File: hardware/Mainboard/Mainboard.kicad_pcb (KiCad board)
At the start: 2 copper layers, 160 x 160 mm, 83 parts, among them IC1 74HC138, IC10 FT232RL, IC11 TL7702A, IC2 W65C02, IC3 74HC00, IC4 SYSTEM ROM, IC5 W65C22, IC6 RAM, IC7 W65C22, IC8 W65C51, IC9 74HC148, SW1 CARRIER, SW2 PORT B, SW3 INTERRUPT, SW4 CLOCK INPUT, SW5 NMI, SW6 FT232 RESET, SW7 RESET, T1 BC546, U1 R-785.0-1.0, X1 EXPANSION, X2 TIMER, X3 KEYBOARD, X4 EXT. CLOCK, X5 SERIAL, X6 GND, X7 DC IN, X8 PORT B

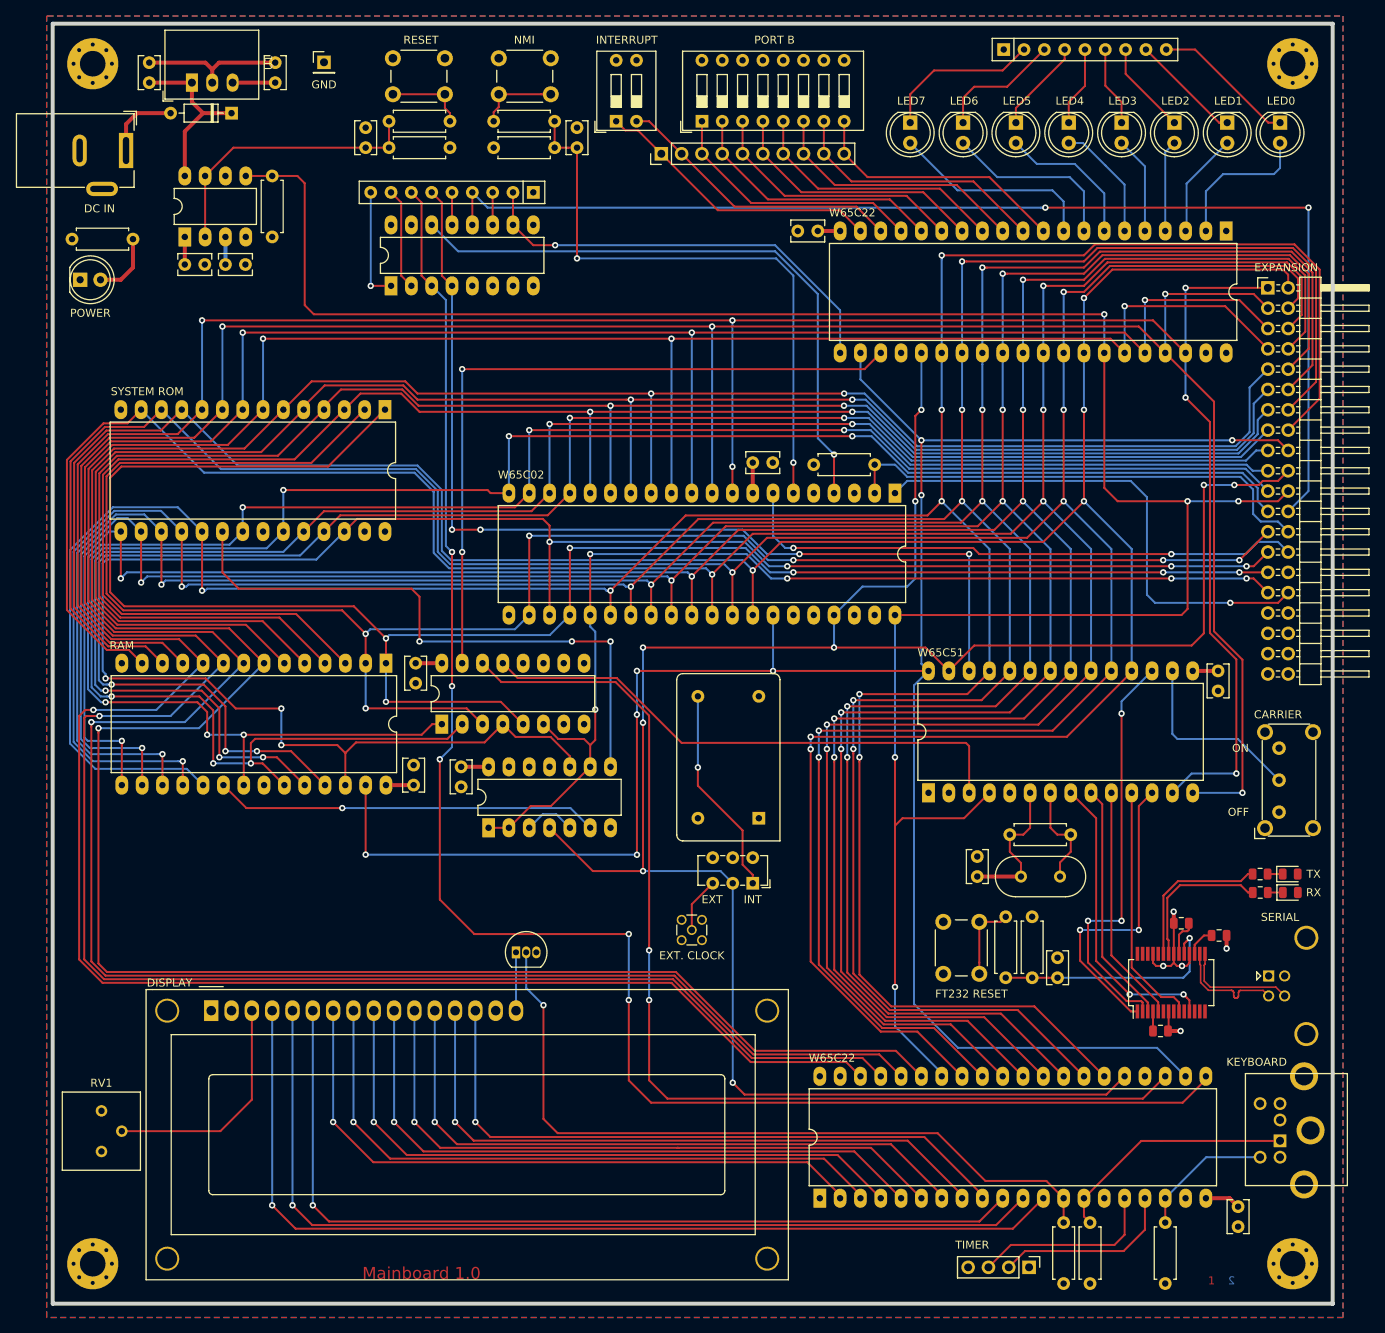
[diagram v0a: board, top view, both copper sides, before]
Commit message: Hardware: 	- Add pull up resistor for PB
Documentation:
	- Add more datasheets
	- Update documentation

Misc:
	- Rename CHANGELOG
	- Remove old files

Signed-off-by: Daniel Kampert <DanielKampert@kampis-elektroecke.de>
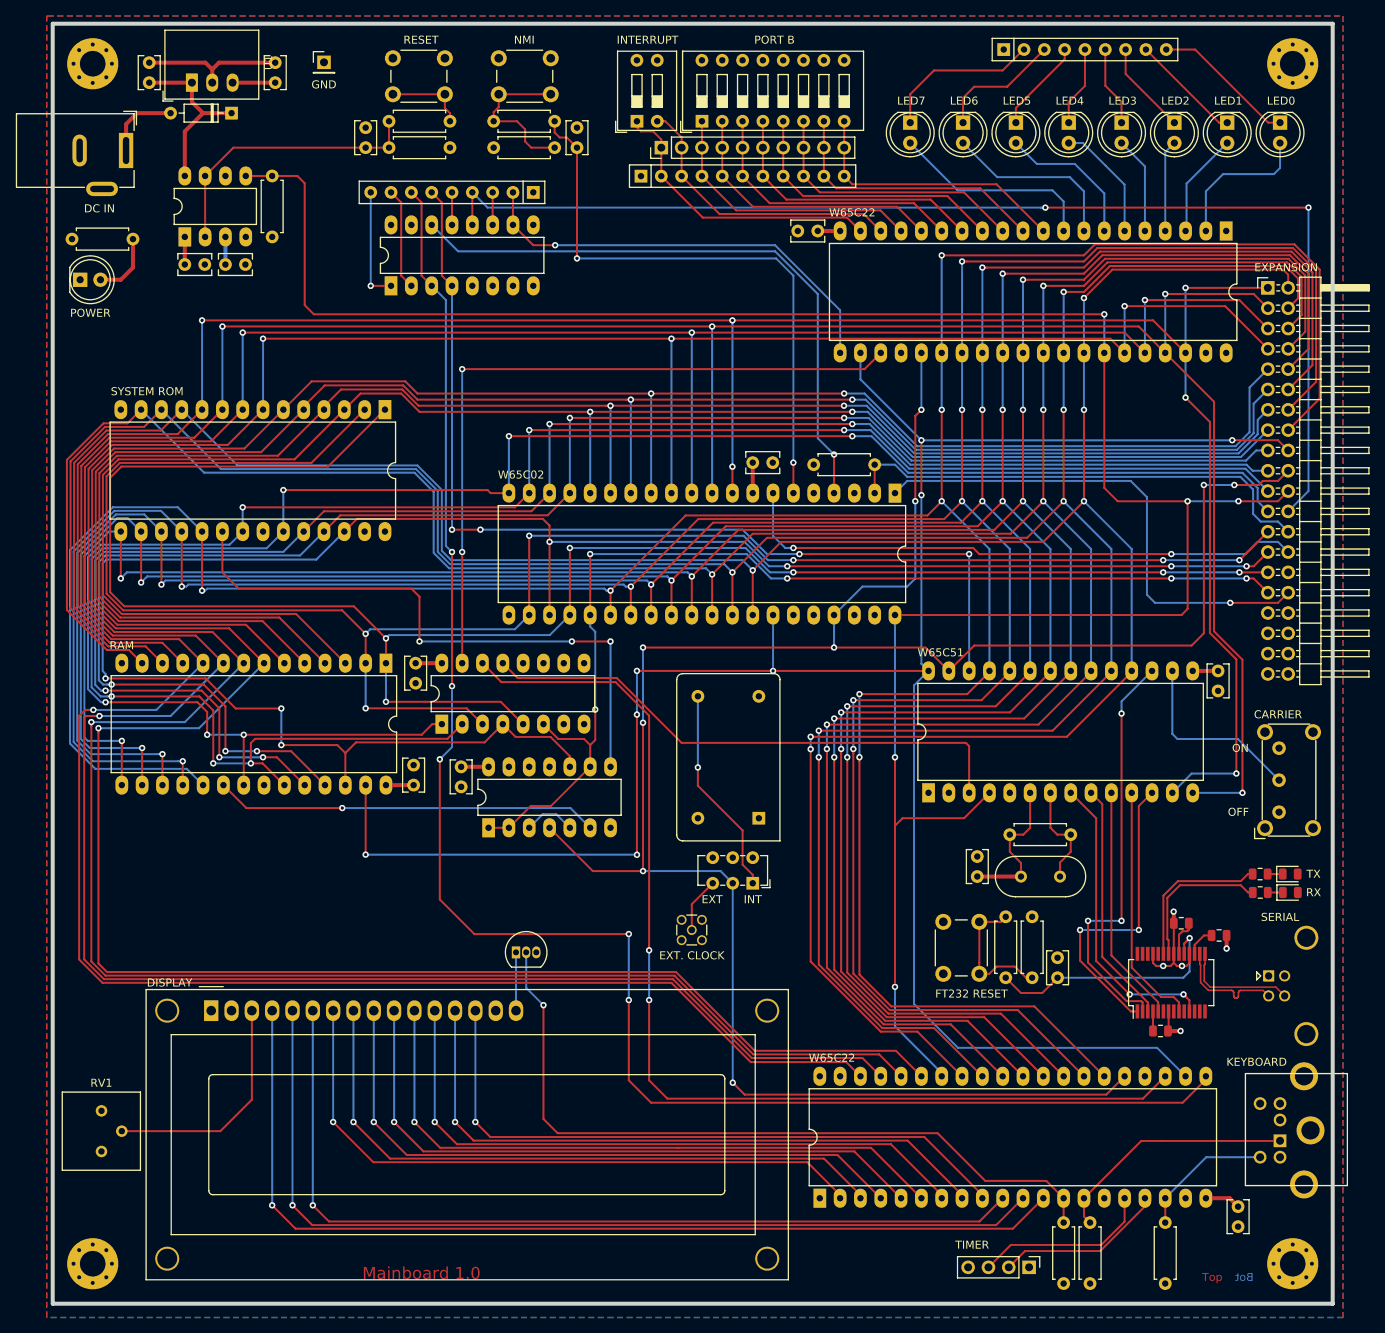
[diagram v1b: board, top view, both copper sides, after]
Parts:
- added RN1: 4k7, Resistor_THT:R_Array_SIP11, F.Cu at (211.6, 70.4)
- R1: value 4,7k -> 4k7
- moved SW3 2.59 mm to (211.1, 63.5)
- moved X1 0.76 mm to (214.1, 66.8)
- renumbered C2 to C1, C1 to C2, R9 to R10, R14 to R11, R10 to R12, R11 to R13, R15 to R14, R12 to R15, R13 to R7, R7 to R8, R8 to R9, RN1 to RN2, RN2 to RN3, X8 to X1, X1 to X2, X2 to X3, X3 to X4, X4 to X5, X5 to X6, X6 to X7, X7 to X8
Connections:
- IC1 pad 10: (no net) -> Net-(IC1-Pad10)
- IC1 pad 11: (no net) -> Net-(IC1-Pad11)
- IC1 pad 12: (no net) -> Net-(IC1-Pad12)
- IC1 pad 7: (no net) -> Net-(IC1-Pad7)
- IC1 pad 9: (no net) -> Net-(IC1-Pad9)
- IC10 pad 10: (no net) -> Net-(IC10-Pad10)
- IC10 pad 12: (no net) -> Net-(IC10-Pad12)
- IC10 pad 13: (no net) -> Net-(IC10-Pad13)
- IC10 pad 14: (no net) -> Net-(IC10-Pad14)
- IC10 pad 26: (no net) -> Net-(IC10-Pad26)
- IC10 pad 27: (no net) -> Net-(IC10-Pad27)
- IC10 pad 28: (no net) -> Net-(IC10-Pad28)
- IC10 pad 6: (no net) -> Net-(IC10-Pad6)
- IC11 pad 6: (no net) -> Net-(IC11-Pad6)
- IC2 pad 3: (no net) -> Net-(IC2-Pad3)
- IC2 pad 35: (no net) -> Net-(IC2-Pad35)
- IC2 pad 39: (no net) -> Net-(IC2-Pad39)
- IC2 pad 5: (no net) -> Net-(IC2-Pad5)
- IC5 pad 15: (no net) -> Net-(IC5-Pad15)
- IC5 pad 19: (no net) -> Net-(IC5-Pad19)
- IC5 pad 39: (no net) -> Net-(IC5-Pad39)
- IC5 pad 40: (no net) -> Net-(IC5-Pad40)
- IC7 pad 39: (no net) -> Net-(IC7-Pad39)
- IC7 pad 40: (no net) -> Net-(IC7-Pad40)
- IC8 pad 5: (no net) -> Net-(IC8-Pad5)
- IC9 pad 15: (no net) -> Net-(IC9-Pad15)
- IC9 pad 6: (no net) -> Net-(IC9-Pad6)
- IC9 pad 7: (no net) -> Net-(IC9-Pad7)
- IC9 pad 9: (no net) -> Net-(IC9-Pad9)
- R10 pad 2: /Supply/~Reset_FT232 -> Net-(R10-Pad2)
- R11 pad 2: Net-(R14-Pad2) (its old number) -> Net-(R10-Pad2)
- R6 pad 2: /IRQ/~NMI -> Net-(R6-Pad2)
- R7 pad 2: Net-(R13-Pad2) -> Net-(R6-Pad2)
- RV1 pad 3: (no net) -> Net-(RV1-Pad3)
- SW5 pad 2: Net-(R13-Pad2) -> Net-(R6-Pad2)
- SW6 pad 2: Net-(R14-Pad2) (its old number) -> Net-(R10-Pad2)
- X2 pad 30: (no net) -> Net-(X2-Pad30)
- X2 pad 33: (no net) -> Net-(X2-Pad33)
- X2 pad 34: (no net) -> Net-(X2-Pad34)
- X2 pad 35: (no net) -> Net-(X2-Pad35)
- X2 pad 36: (no net) -> Net-(X2-Pad36)
- X2 pad 37: (no net) -> Net-(X2-Pad37)
- X2 pad 38: (no net) -> Net-(X2-Pad38)
- X4 pad 2: (no net) -> Net-(X4-Pad2)
- X4 pad 6: (no net) -> Net-(X4-Pad6)
- X6 pad 1: (no net) -> Net-(X6-Pad1)
- XTAL1 pad 1: (no net) -> Net-(XTAL1-Pad1)
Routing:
- net Net-(R6-Pad2): track 0.00 -> 20.0 mm
- net Net-(R10-Pad2): track 0.00 -> 17.6 mm
- net Net-(R13-Pad2): track 10.1 -> 0.00 mm
- net Net-(R14-Pad2) (its old number): track 10.1 -> 0.00 mm
- net /LCD / PS2/Timer0: track 22.9 -> 21.2 mm
- net /IO/PB6: track 33.0 -> 34.6 mm
- net /IO/PB5: track 33.0 -> 34.6 mm
- net /IO/PB4: track 33.0 -> 34.6 mm
- net /IO/PB7: track 33.0 -> 34.6 mm
- net /IO/PB3: track 33.0 -> 34.6 mm
- net /IO/PB2: track 33.0 -> 34.6 mm
- net /IO/PB1: track 33.0 -> 34.6 mm
- net /IO/PB0: track 33.0 -> 34.6 mm
- net /Supply/~Reset_FT232: track 29.7 -> 31.3 mm
- net /IRQ/~NMI: track 75.1 -> 73.9 mm
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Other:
- board text added: "Bot"
- board text added: "Top"
- board text removed: "1"
- board text removed: "2"
